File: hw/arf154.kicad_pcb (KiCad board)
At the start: 4 copper layers, 29 parts, among them P1 Cn1, P2 Cn2, P3 CONN_02X05, P4 USB_B, SW1 SW_PUSH, T1 2450BM15A0015, U1 ATSAMR21G1x, U2 AZ1117C, Y1 16MHz

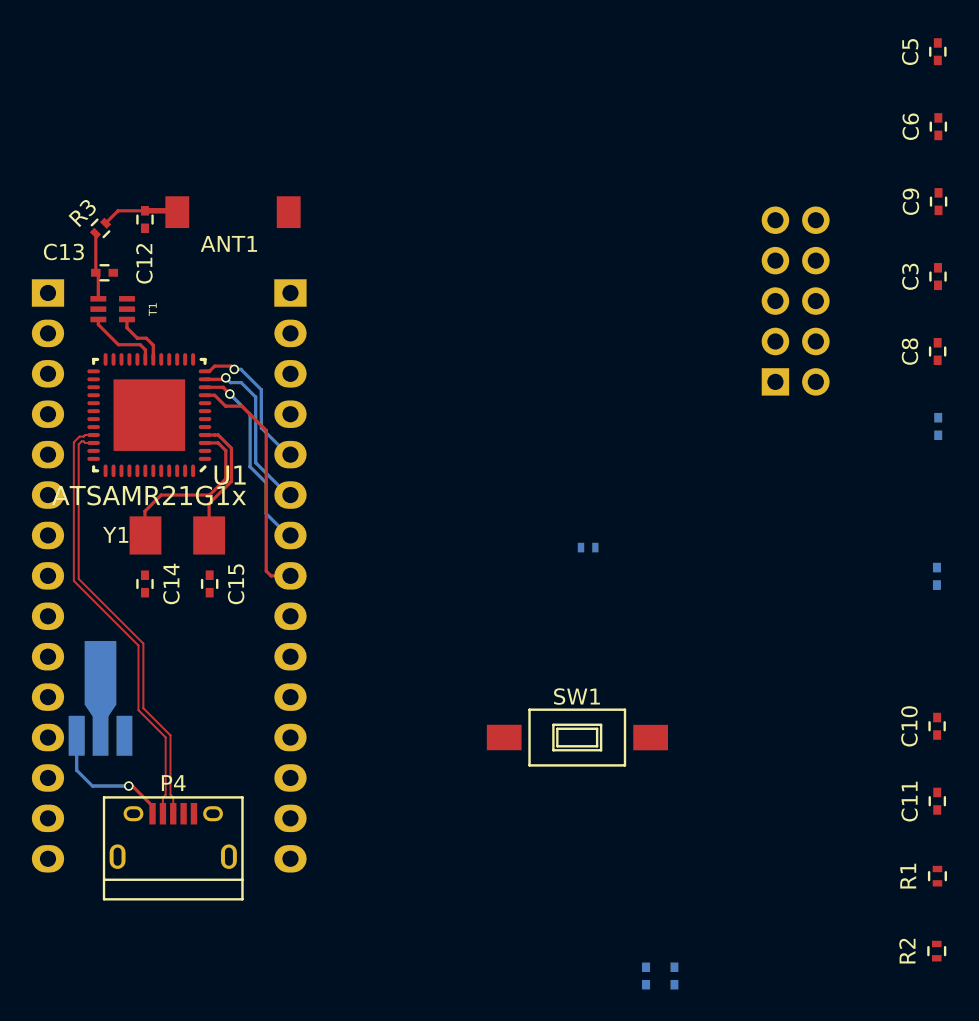
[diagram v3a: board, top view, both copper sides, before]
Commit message: Layout for the analog pads and DRC fix on the USB signals
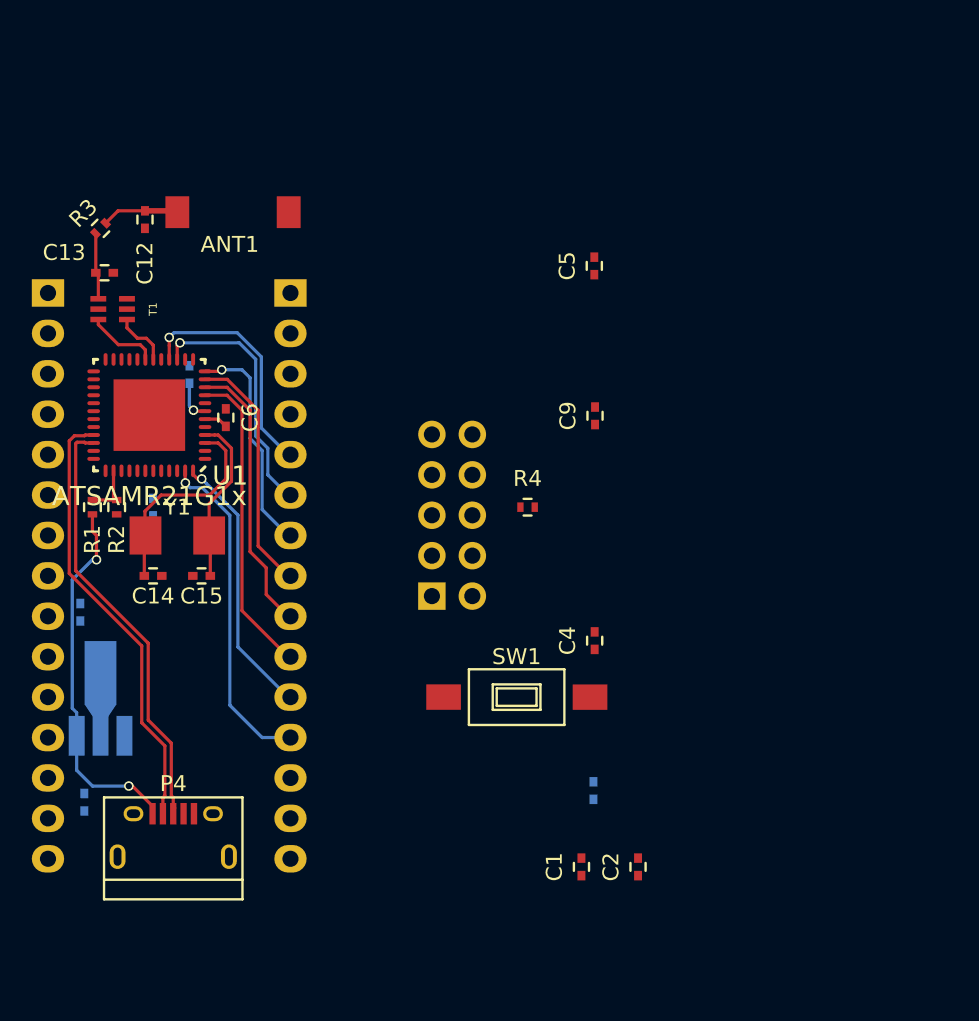
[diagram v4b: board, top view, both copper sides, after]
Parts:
- C1, C2, C4, R4: moved to F.Cu
- C10, C11, C3, C8: moved to B.Cu
- moved R2 58.6 mm to (114.8, 97.3), turned to 270 degrees
- moved R1 58.0 mm to (113.3, 97.3)
- moved C11 55.2 mm to (112.5, 103.9)
- moved C10 53.8 mm to (112.8, 115.8), turned to 270 degrees
- moved C3 51.4 mm to (117.1, 97.3), turned to 270 degrees
- moved C6 48.4 mm to (121.7, 91.7)
- moved C8 47.0 mm to (119.4, 88.9)
- moved C4 25.4 mm to (144.8, 105.7), turned to 90 degrees
- moved C7 25.4 mm to (144.8, 115.1)
- moved P3 25.4 mm to (134.6, 102.9)
- moved C5 25.4 mm to (144.8, 82.1)
- moved C9 25.4 mm to (144.9, 91.5)
- moved C1 7.97 mm to (144.0, 119.9), turned to 90 degrees
- moved C2 7.23 mm to (147.6, 119.9), turned to 90 degrees
- moved R4 4.58 mm to (140.6, 97.3)
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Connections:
- P2 pad 10: /MainProcessor/PA9 -> /MainProcessor/PA4
- P2 pad 11: /MainProcessor/PB2 -> /MainProcessor/PB3
- P2 pad 12: /MainProcessor/PB3 -> /MainProcessor/PB2
- P2 pad 5: /MainProcessor/PA7 -> /MainProcessor/PA9
- P2 pad 6: /MainProcessor/PA6 -> /MainProcessor/PA8
- P2 pad 7: /MainProcessor/PA5 -> /MainProcessor/PA7
- P2 pad 8: /MainProcessor/PA4 -> /MainProcessor/PA6
- P2 pad 9: /MainProcessor/PA8 -> /MainProcessor/PA5
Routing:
- net /MainProcessor/PB2: track 0.00 -> 21.0 mm, vias 0 -> 1
- net /MainProcessor/PB3: track 0.00 -> 17.0 mm, vias 0 -> 1
- net /MainProcessor/PA8: track 0.00 -> 15.8 mm, vias 0 -> 1
- net /MainProcessor/PA9: track 0.00 -> 15.1 mm, vias 0 -> 1
- net VCC: track 8.35 -> 23.3 mm, vias 1 -> 2
- net /MainProcessor/PA5: track 12.3 -> 17.5 mm, vias 1 -> 0
- net /MainProcessor/PA7: track 9.22 -> 14.4 mm
- net /MainProcessor/PA6: track 10.9 -> 15.5 mm, vias 1 -> 0
- net /MainProcessor/PA4: track 15.3 -> 19.6 mm
- net VAA: track 0.00 -> 4.04 mm, vias 0 -> 1
- net /MainProcessor/PA23: track 0.00 -> 3.44 mm
- net Net-(C15-Pad1): track 8.11 -> 10.7 mm
- net Net-(C14-Pad1): track 10.7 -> 13.3 mm
- net /Sheet557215E3/D+: track 27.5 -> 28.0 mm

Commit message: Layout updated, need improvement on ground layers and a power switch
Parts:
- added D1: PRTR5V0U2X, comm:SOT143B, B.Cu at (120.7, 112.8)
- P3: footprint Pin_Headers:Pin_Header_Straight_2x05 -> processing:CMxDBG; moved to F.Cu
- SW1: footprint Buttons_Switches_SMD:SW_SPST_FSMSM -> processing:tactileswitch
- moved C4 32.2 mm to (122.4, 82.5)
- moved C1 30.7 mm to (113.8, 114.5)
- moved C9 26.6 mm to (119.9, 82.5)
- moved SW1 25.9 mm to (114.0, 109.0), turned to 270 degrees
- moved C2 25.0 mm to (123.2, 114.3)
- moved C7 22.2 mm to (122.7, 112.5)
- moved C5 22.2 mm to (122.9, 85.6), turned to 180 degrees
- moved R4 20.5 mm to (122.9, 87.1), turned to 180 degrees
- moved P3 14.6 mm to (120.7, 107.2)
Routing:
- net /MainProcessor/RST: track 0.00 -> 44.9 mm, vias 0 -> 2
- net /MainProcessor/SWCLK: track 0.00 -> 18.8 mm, vias 0 -> 2
- net VDD: track 0.00 -> 15.0 mm, vias 0 -> 4
- net /Sheet557215E3/D-: track 27.6 -> 39.8 mm, vias 0 -> 2
- net /Sheet557215E3/D+: track 28.0 -> 40.2 mm, vias 0 -> 2
- net /MainProcessor/SWDIO: track 0.00 -> 11.3 mm, vias 0 -> 2
- net GND: track 0.00 -> 5.77 mm, vias 0 -> 3
- net /MainProcessor/PB2: track 21.0 -> 19.9 mm
- net Net-(C14-Pad1): track 13.3 -> 12.3 mm
- added copper zone on B.Cu, net GND
- added copper zone on F.Cu, net GND
- added copper zone on In2.Cu, net VDD
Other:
- board outline added: 18.3 x 46.2 mm

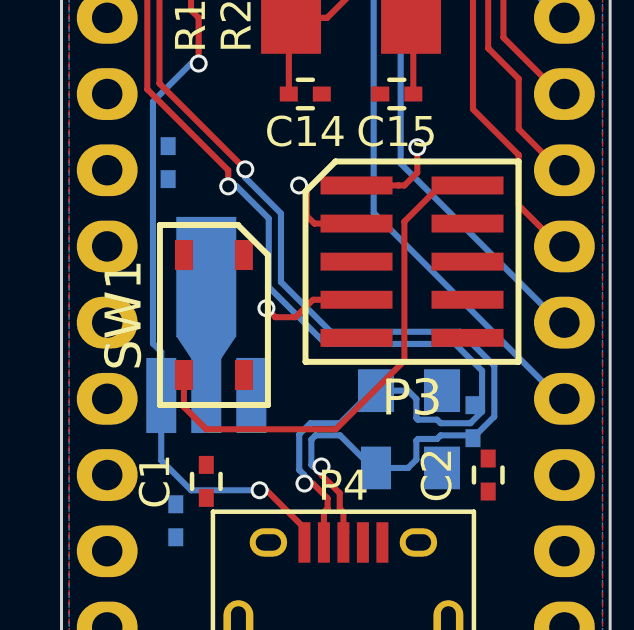
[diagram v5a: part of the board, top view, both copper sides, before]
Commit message: Layout modifications
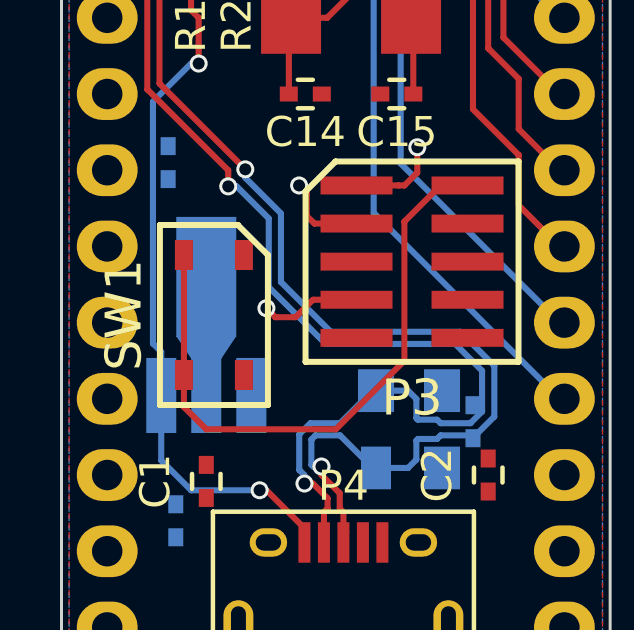
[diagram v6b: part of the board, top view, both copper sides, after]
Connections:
- U1 pad 37: /MainProcessor/PA22 -> /MainProcessor/PB22
- U1 pad 38: /MainProcessor/PA23 -> /MainProcessor/PB23
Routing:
- net GND: track 5.77 -> 36.5 mm, vias 3 -> 4
- net /Sheet557215E3/D-: track 39.8 -> 9.06 mm, vias 2 -> 1
- net /MainProcessor/RST: track 44.9 -> 48.9 mm
- net /MainProcessor/PB23: track 0.00 -> 1.64 mm
- net /MainProcessor/PA23: track 3.44 -> 1.80 mm
